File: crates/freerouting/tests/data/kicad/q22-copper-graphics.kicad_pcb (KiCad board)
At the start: 2 copper layers, 30 x 20 mm, 2 parts, among them J1 x, P1 x

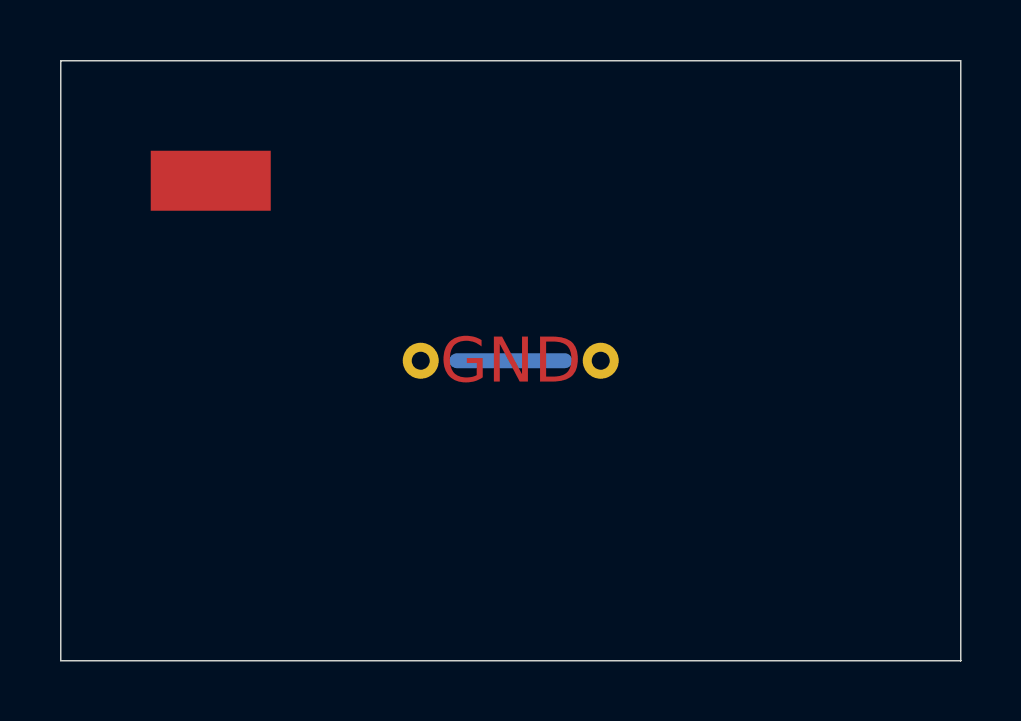
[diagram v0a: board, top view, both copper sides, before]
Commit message: feat: copper shapes of a net are fixed copper of that net (Q22.4)
KiCad's DSN export leaves out copper shapes. Q22.4's first landing made
shapes of no net keepouts, and left out shapes of a listed net. Those now
become fixed conduction areas of their net, in the plugin's fix-ups and the
.kicad_pcb reader alike. Their own net connects through them, and other nets
can't cross them.

- DSN: a wire may carry (attr obstacle). Both writers write it back only
  when it is set, so a DSN without it reads exactly as before.
- Engine: an area wire with that attribute is inserted by
  insert_fixed_copper_area, a conduction area that stays an obstacle to
  other nets even with plane_as_obstacle=false. Two fixed areas of one net
  that touch count as connected, so a shape's pieces form one endpoint.
- The areas are type fix, so the session writer drops them, and
  final_copper writes traces and vias only. Q20's output check treats a
  trace crossing one as a routed clearance breach.

Graded through the plugin export at the router's 270 s cap. Routing-caused
copper errors are 0 everywhere. KiCad unconnected, this change against main:
vfo 14/13 (1.1 s against 17.8 s), miniscope 67/61, openair 58/63; openair
uncapped reaches 31. Miniscope's cost is new item Q22.17. Connection parity
is 7 of 7 exact.

Co-Authored-By: Claude Opus 5.5 <noreply@anthropic.com>
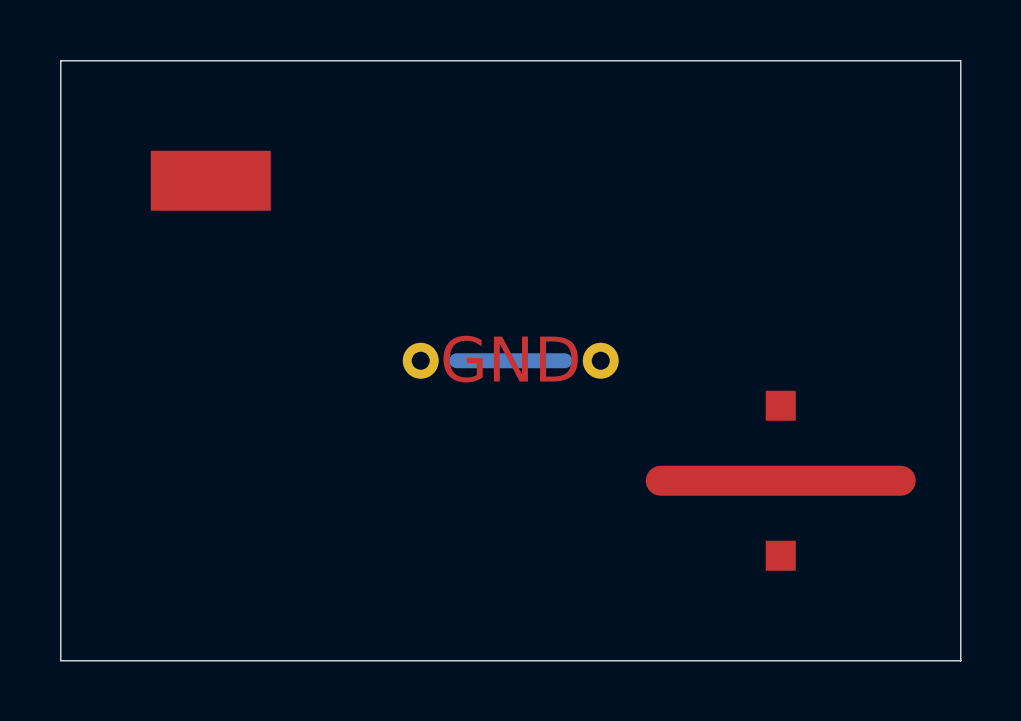
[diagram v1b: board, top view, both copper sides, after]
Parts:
- added J2: x, l:smdjumper, F.Cu at (24.0, 14.0)
- added P2: x, l:pad, F.Cu at (6.00, 4.00)
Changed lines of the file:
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@@
   (net 1 "N2")
   (net 2 "FG")
+  (net 3 "N3")
   (gr_rect (start 0 0) (end 30 20) (stroke (width 0.05) (type solid)) (fill none) (layer "Edge.Cuts"))
   (footprint "l:jumper" (layer "F.Cu") (at 15 10)
@@
     (property "Reference" "P1") (property "Value" "x")
     (pad "1" smd rect (at 0 0) (size 1 1) (layers "F.Cu" "F.Mask") (net 2 "FG")))
+  (footprint "l:pad" (layer "F.Cu") (at 6 4)
+    (property "Reference" "P2") (property "Value" "x")
+    (pad "1" smd rect (at 0 0) (size 1 1) (layers "F.Cu" "F.Mask") (net 2 "FG")))
   (gr_poly (pts (xy 3 3) (xy 7 3) (xy 7 5) (xy 3 5)) (stroke (width 0) (type solid)) (fill solid) (layer "F.Cu") (net 2))
+  (footprint "l:smdjumper" (layer "F.Cu") (at 24 14)
+    (property "Reference" "J2") (property "Value" "x")
+    (pad "1" smd rect (at 0 -2.5) (size 1 1) (layers "F.Cu" "F.Mask") (net 3 "N3"))
+    (pad "2" smd rect (at 0 2.5) (size 1 1) (layers "F.Cu" "F.Mask") (net 3 "N3")))
+  (gr_line (start 20 14) (end 28 14) (stroke (width 1) (type solid)) (layer "F.Cu") (net 2))
 )
